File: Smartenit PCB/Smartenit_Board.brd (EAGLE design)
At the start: 54.9 x 71.8 mm, 86 parts, among them J1 2X5CONNECTOR1.27MM, Q1 QUARTZ_3.58M_2PIN, U1 SN74LVC1G3157, U2 ADE7953, U3 ESP-WROOM-32

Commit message: Fixed Silk Screen final before sending to Al
fixed silk screen and renumbered parts
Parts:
- renumbered LD100 to R/G_LED, LED100 to BLUE_LED
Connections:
- net ADC1 renamed PILOT_READ
- net DIO0 renamed CS
- net DIO1 renamed MPLEX
- net DIO10 renamed GFI_TEST
- net DIO13 renamed PILOT_GEN
- net DIO16 renamed GREEN_LED
- net DIO17 renamed RED_LED
- net DIO8 renamed BUTTON
- net DIO9 renamed BLUE_LED
- net N$30 renamed GPIO2
- net 3.3V: no longer R15.1
- net GND: now also R15.1
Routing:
- net 3.3V: track 221.8 -> 217.6 mm
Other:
- board text added: "C:/Users/Brandon/Desktop/Fall 2017/EECS 159A (SENIOR DESIGN)/chipart_00000.bmp"

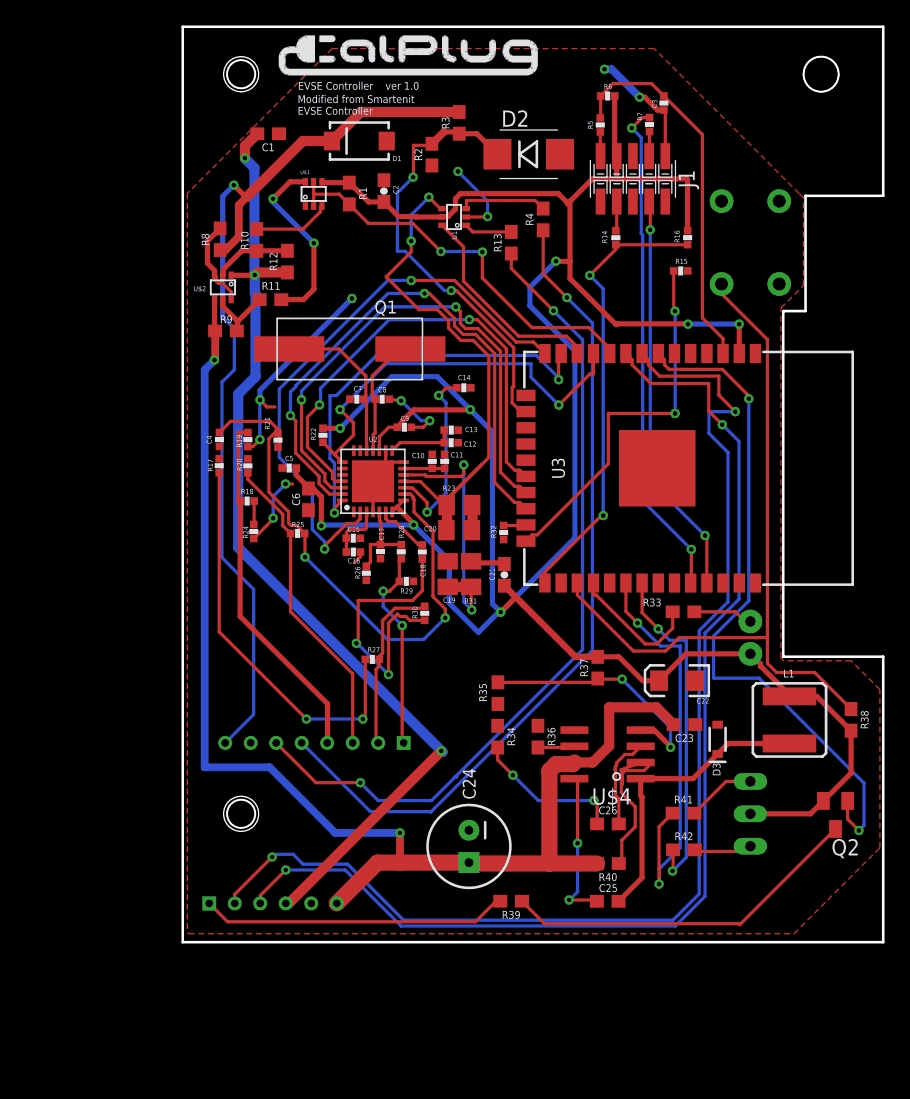
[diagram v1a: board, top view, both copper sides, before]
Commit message: Changed ground planes
separated into analog and digital grounds. Rearachnged layout for better coupling.
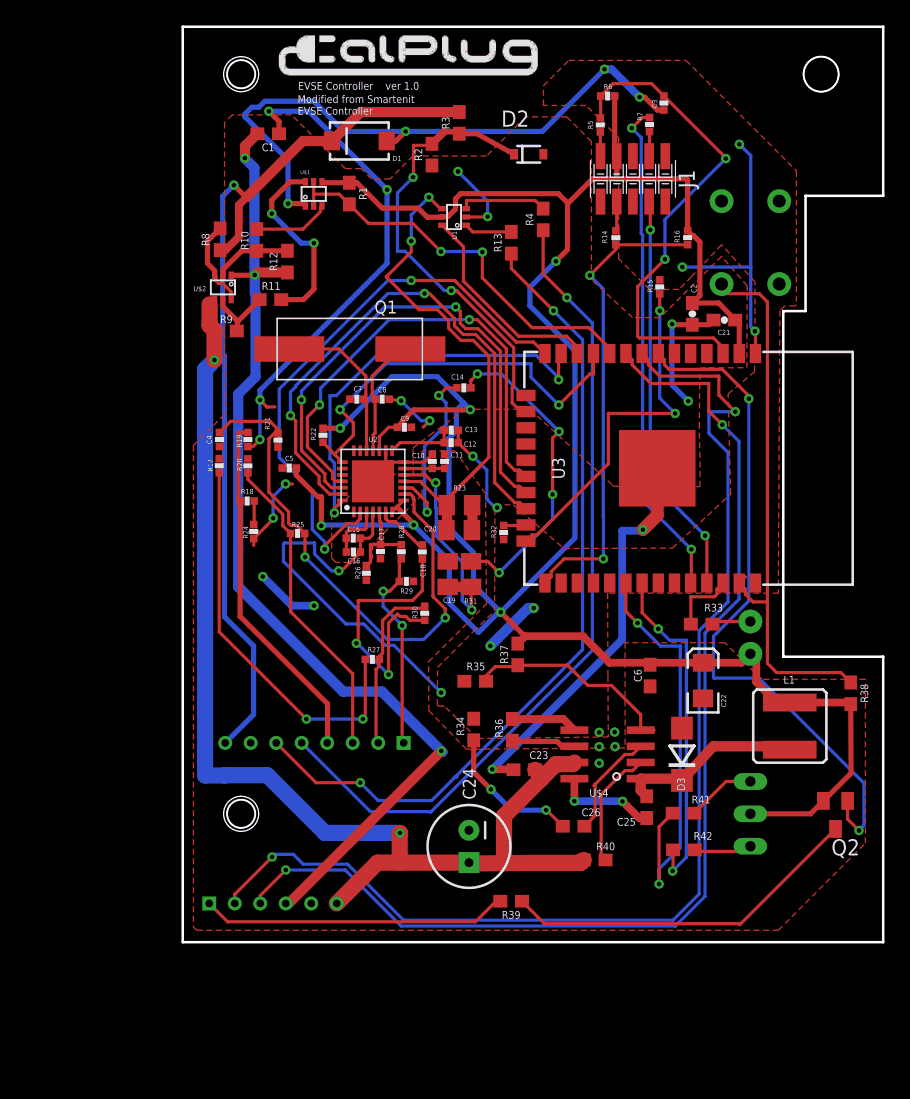
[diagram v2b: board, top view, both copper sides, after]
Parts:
- C22: value (none) -> 10uF
- C24: value (none) -> 100uF
- D2: device SparkFun:DIODE-HV -> SparkFun:SOD-323
- D3: device SparkFun-DiscreteSemi:SOD-323 -> diode:DO214BA
- moved C6 30.1 mm to (36.7, -50.9)
- moved C21 26.4 mm to (42.5, -23.0), turned to 180 degrees
- moved C2 26.0 mm to (40.0, -22.5), turned to 270 degrees
- moved C23 13.0 mm to (26.8, -58.3), turned to 0 degrees
- moved C25 8.00 mm to (36.4, -61.2), turned to 90 degrees
- moved R37 6.36 mm to (26.3, -49.2)
- moved D3 3.03 mm to (39.2, -57.1)
- moved C26 2.70 mm to (30.7, -62.7)
- moved R38 2.08 mm to (52.4, -52.3)
- moved R36 2.08 mm to (25.9, -55.1)
- moved R15 2.07 mm to (37.4, -20.4), turned to 270 degrees
- moved C22 2.05 mm to (40.8, -51.3), turned to 90 degrees
- moved R35 2.01 mm to (22.9, -51.3), turned to 0 degrees
- moved R34 1.96 mm to (22.8, -55.1)
- moved R33 1.72 mm to (40.7, -46.9)
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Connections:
- removed net GND: C1.1, C10.2, C11.2, C12.1, C13.1, C14.2, C15.1, C16.1, C17.1, C18.2, C19.2, C2.2, C20.2, C21.2, C22.C, C23.1, C24.2, C3.1, C4.1, C5.1, C6.1, C7.1, C8.1, C9.1, D1.A, D2.A, D3.A, J1.10, R15.1, R17.2, R19.2, R2.1, R20.1, R21.1, R23.2, R24.2, R26.1, R29.1, R30.2, R31.2, R32.1, R34.1, R35.1, R36.1, S100.1, U$1.1, U$3.7, U$4.5, U$5.5, U1.2, U2.14, U2.16, U2.4, U2.PAD, U3.1, U3.15, U3.38, U3.GND
- new net AGND: C1.1, C10.2, C11.2, C14.2, C17.1, C18.2, C19.2, C2.2, C20.2, C21.2, C22.C, C23.1, C24.2, C4.1, C5.1, C6.1, C7.1, C8.1, C9.1, D2.2, D3.A, R17.2, R19.2, R2.1, R20.1, R21.1, R23.2, R24.2, R26.1, R29.1, R30.2, R31.2, U$3.7, U$5.5, U1.2, U2.14, U2.16, U2.PAD, U3.15, U3.GND
- new net DGND: C12.1, C13.1, C15.1, C16.1, C3.1, D1.A, J1.10, R15.1, R32.1, R34.1, R35.1, R36.1, S100.1, U$1.1, U$4.5, U2.4, U3.1, U3.38
- net BLUE_LED: now also U3.36; no longer U3.28
- net BUTTON: now also U3.37; no longer U3.27
- net PILOT_READ: now also D2.1; no longer D2.C
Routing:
- net AGND: track 0.00 -> 164.2 mm, vias 0 -> 22
- net DGND: track 0.00 -> 119.2 mm, vias 0 -> 13
- net GND: track 81.8 -> 0.00 mm, vias 13 -> 0
- net BUTTON: track 57.4 -> 43.9 mm
- net NRST: track 29.6 -> 38.7 mm, vias 0 -> 2
- net N$18: track 23.2 -> 14.6 mm
- net 12V: track 100.2 -> 93.1 mm
- net BLUE_LED: track 10.5 -> 5.35 mm
- net 3.3V: track 217.6 -> 212.8 mm, vias 8 -> 6
- net N$14: track 13.5 -> 9.42 mm
- net N$22: track 12.1 -> 8.34 mm
- net V2P: track 20.9 -> 17.6 mm
- net N$19: track 19.8 -> 16.8 mm, vias 2 -> 0
- net N$4: track 2.90 -> 5.18 mm
- net GPIO0: track 35.4 -> 37.2 mm
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- added copper zone on layer 1, net AGND
- added copper zone on layer 1, net DGND
- removed copper zone on layer 1, net GND

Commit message: minor changes to ground planes
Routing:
- net AGND: track 164.2 -> 149.1 mm
- net DGND: track 119.2 -> 104.3 mm
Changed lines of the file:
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@@
 <contactref element="C4" pad="2"/>
 <contactref element="U2" pad="9"/>
-<via x="9.59" y="-41.59" extent="1-16" drill="0.35"/>
 <wire x1="19.648" y1="-44.71751875" x2="19.648" y2="-44.658" width="0.254" layer="1"/>
 <wire x1="19.648" y1="-44.658" x2="19.63" y2="-44.64" width="0.254" layer="1"/>
@@
 <wire x1="19.63" y1="-39.55" x2="18.14" y2="-38.06" width="0.254" layer="1"/>
 <wire x1="18.14" y1="-37.07560625" x2="18.14" y2="-38.06" width="0.254" layer="1"/>
-<wire x1="9.59" y1="-41.59" x2="9.59" y2="-39.77" width="0.254" layer="1"/>
-<wire x1="9.59" y1="-39.77" x2="9.56" y2="-39.74" width="0.254" layer="1"/>
+<wire x1="9.59" y1="-39.77" x2="9.5734" y2="-39.7534" width="0.254" layer="1"/>
+<wire x1="9.5734" y1="-39.7534" x2="9.56" y2="-39.74" width="0.254" layer="1"/>
 <wire x1="2.88" y1="-31.82" x2="3.75" y2="-30.95" width="0.254" layer="1"/>
 <wire x1="3.75" y1="-30.95" x2="6.84" y2="-30.95" width="0.254" layer="1"/>
@@
 <wire x1="6.7584" y1="-32.31" x2="7.2084" y2="-31.86" width="0.254" layer="1"/>
 <wire x1="7.2084" y1="-31.86" x2="7.47" y2="-31.86" width="0.254" layer="1"/>
-<wire x1="9.59" y1="-41.59" x2="16.06" y2="-48.06" width="0.254" layer="16"/>
-<wire x1="18.89" y1="-48.06" x2="20.59" y2="-46.36" width="0.254" layer="16"/>
-<wire x1="16.06" y1="-48.06" x2="18.89" y2="-48.06" width="0.254" layer="16"/>
+<wire x1="20.59" y1="-46.36" x2="18.89" y2="-48.06" width="0.254" layer="16"/>
 <wire x1="18.0752" y1="-36.864225" x2="18.0752" y2="-37.01080625" width="0.254" layer="1"/>
 <wire x1="17.32" y1="-36.651" x2="17.861975" y2="-36.651" width="0.254" layer="1"/>
@@
 <wire x1="8.3072" y1="-38.05061875" x2="6.7584" y2="-36.50181875" width="0.254" layer="1"/>
 <wire x1="6.7584" y1="-36.50181875" x2="6.7584" y2="-32.31" width="0.254" layer="1"/>
+<wire x1="18.89" y1="-48.06" x2="16.82" y2="-48.06" width="0.254" layer="16"/>
+<wire x1="16.82" y1="-48.06" x2="14.3414" y2="-45.6322" width="0.254" layer="16"/>
+<via x="14.3414" y="-45.6322" extent="1-16" drill="0.35"/>
+<wire x1="14.3414" y1="-45.6322" x2="12.8154" y2="-45.6322" width="0.254" layer="1"/>
+<wire x1="12.8154" y1="-45.6322" x2="9.6012" y2="-42.418" width="0.254" layer="1"/>
+<wire x1="9.6012" y1="-42.418" x2="9.6012" y2="-39.7812" width="0.254" layer="1"/>
+<wire x1="9.6012" y1="-39.7812" x2="9.59" y2="-39.77" width="0.254" layer="1"/>
 </signal>
 <signal name="N$11">
@@
 <wire x1="5.015" y1="-13.365" x2="9.42" y2="-8.96" width="0.8" layer="1"/>
 <wire x1="9.42" y1="-8.96" x2="11.7" y2="-8.96" width="0.8" layer="1"/>
-<wire x1="11.7" y1="-8.96" x2="13.97" y2="-6.69" width="0.8" layer="1"/>
+<wire x1="11.7" y1="-8.96" x2="12.5906" y2="-8.0694" width="0.8" layer="1"/>
+<wire x1="12.5906" y1="-8.0694" x2="13.97" y2="-6.69" width="0.8" layer="1"/>
 <wire x1="13.97" y1="-6.69" x2="21.69" y2="-6.69" width="0.8" layer="1"/>
 <wire x1="3.13" y1="-22.76" x2="3.13" y2="-25.67040625" width="0.4064" layer="16"/>
@@
 <contactref element="R26" pad="1"/>
 <contactref element="R17" pad="2"/>
-<wire x1="18.791" y1="-41.744" x2="18.791" y2="-44.229" width="0.254" layer="1"/>
-<wire x1="18.02" y1="-45" x2="13.76" y2="-45" width="0.254" layer="1"/>
-<wire x1="13.76" y1="-45" x2="13.76" y2="-48.22" width="0.254" layer="1"/>
 <wire x1="13.76" y1="-48.22" x2="13.62" y2="-48.36" width="0.254" layer="1"/>
 <via x="13.62" y="-48.36" extent="1-16" drill="0.35"/>
 <wire x1="13.62" y1="-48.36" x2="13.69" y2="-48.36" width="0.254" layer="16"/>
-<wire x1="13.69" y1="-48.36" x2="16.14" y2="-50.81" width="0.254" layer="16"/>
 <via x="16.14" y="-50.81" extent="1-16" drill="0.35"/>
 <wire x1="16.14" y1="-50.81" x2="16.14" y2="-46.76" width="0.254" layer="1"/>
@@
 <wire x1="17.50343125" y1="-46.2516" x2="17.80183125" y2="-46.55" width="0.254" layer="1"/>
 <wire x1="17.80183125" y1="-46.55" x2="18.98" y2="-46.55" width="0.254" layer="1"/>
-<wire x1="18.791" y1="-44.229" x2="18.02" y2="-45" width="0.254" layer="1"/>
 <contactref element="C14" pad="2"/>
 <contactref element="C4" pad="1"/>
@@
 <via x="16.0274" y="-12.7762" extent="1-16" drill="0.35"/>
 <wire x1="6.06" y1="-28.52" x2="16.0274" y2="-18.5526" width="0.4064" layer="16"/>
-<wire x1="16.0274" y1="-12.7762" x2="9.8806" y2="-6.6294" width="0.4064" layer="16"/>
-<wire x1="9.8806" y1="-6.6294" x2="6.7564" y2="-6.6294" width="0.4064" layer="16"/>
-<via x="6.7564" y="-6.6294" extent="1-16" drill="0.35"/>
-<wire x1="6.7564" y1="-6.6294" x2="7.55" y2="-7.423" width="0.4064" layer="1"/>
 <wire x1="7.55" y1="-7.423" x2="7.55" y2="-8.39" width="0.4064" layer="1"/>
 <wire x1="41.632" y1="-23.0046" x2="41.269" y2="-23.3676" width="0.4064" layer="1"/>
@@
 <wire x1="36.0934" y1="-39.4462" x2="37.22" y2="-38.3196" width="1.016" layer="1"/>
 <wire x1="37.22" y1="-38.3196" x2="37.22" y2="-34.63" width="1.016" layer="1"/>
+<wire x1="13.62" y1="-48.36" x2="16.07" y2="-50.81" width="0.4064" layer="16"/>
+<wire x1="16.07" y1="-50.81" x2="16.14" y2="-50.81" width="0.4064" layer="16"/>
+<wire x1="16.0274" y1="-12.7762" x2="11.1506" y2="-7.8994" width="0.6096" layer="16"/>
+<wire x1="11.1506" y1="-7.8994" x2="9.2202" y2="-7.8994" width="0.6096" layer="16"/>
+<via x="9.2202" y="-7.8994" extent="1-16" drill="0.35"/>
 </signal>
 <signal name="DGND">
@@
 <wire x1="12.462" y1="-42.672" x2="12.2428" y2="-42.672" width="0.254" layer="1"/>
 <via x="12.2428" y="-42.672" extent="1-16" drill="0.35"/>
-<wire x1="12.2428" y1="-42.672" x2="11.6586" y2="-42.672" width="0.254" layer="16"/>
-<wire x1="10.3378" y1="-41.3512" x2="10.3378" y2="-40.4876" width="0.254" layer="16"/>
-<wire x1="10.3378" y1="-40.4876" x2="7.9756" y2="-40.4876" width="0.254" layer="16"/>
-<wire x1="7.9756" y1="-40.4876" x2="7.8994" y2="-40.5638" width="0.254" layer="16"/>
-<wire x1="7.8994" y1="-40.5638" x2="7.8994" y2="-41.9354" width="0.254" layer="16"/>
 <via x="20.2692" y="-52.2224" extent="1-16" drill="0.35"/>
-<wire x1="14.19101875" y1="-46.8376" x2="15.87061875" y2="-48.5172" width="0.254" layer="16"/>
-<wire x1="16.564" y1="-48.5172" x2="20.2692" y2="-52.2224" width="0.254" layer="16"/>
-<wire x1="15.87061875" y1="-48.5172" x2="16.564" y2="-48.5172" width="0.254" layer="16"/>
-<wire x1="12.8016" y1="-46.8376" x2="14.19101875" y2="-46.8376" width="0.254" layer="16"/>
-<wire x1="11.6586" y1="-42.672" x2="10.3378" y2="-41.3512" width="0.254" layer="16"/>
-<wire x1="7.8994" y1="-41.9354" x2="12.8016" y2="-46.8376" width="0.254" layer="16"/>
 <polygon width="0.254" layer="1">
-<vertex x="23.114" y="-55.8292"/>
-<vertex x="20.5232" y="-53.2892"/>
-<vertex x="20.0406" y="-53.2892"/>
-<vertex x="19.9644" y="-53.213"/>
-<vertex x="19.9898" y="-50.2412"/>
-<vertex x="22.8092" y="-47.4218"/>
-<vertex x="24.4602" y="-45.8216"/>
+<vertex x="23.114" y="-55.4736"/>
+<vertex x="20.5994" y="-52.959"/>
+<vertex x="20.5486" y="-52.8066"/>
+<vertex x="20.5486" y="-50.419"/>
+<vertex x="22.9616" y="-47.9552"/>
+<vertex x="24.4602" y="-46.3804"/>
 <vertex x="24.4856" y="-37.4904"/>
 <vertex x="25.9334" y="-37.4904"/>
@@
 <vertex x="46.7106" y="-44.3992"/>
 <vertex x="46.736" y="-44.4246"/>
-<vertex x="33.3248" y="-44.4246"/>
-<vertex x="33.3502" y="-50.9524"/>
-<vertex x="33.3756" y="-55.7022"/>
+<vertex x="31.5214" y="-44.3992"/>
+<vertex x="31.496" y="-50.9524"/>
+<vertex x="31.5214" y="-55.3974"/>
 </polygon>
 <wire x1="21.608" y1="-31.638" x2="21.608" y2="-32.619" width="0.254" layer="1"/>
@@
 <wire x1="9.4284" y1="-13.8684" x2="8.255" y2="-13.8684" width="0.4064" layer="1"/>
 <via x="8.255" y="-13.8684" extent="1-16" drill="0.35"/>
-<wire x1="8.255" y1="-13.8684" x2="8.255" y2="-10.4394" width="0.4064" layer="16"/>
-<wire x1="8.255" y1="-10.4394" x2="4.8768" y2="-7.0612" width="0.4064" layer="16"/>
-<wire x1="4.8768" y1="-7.0612" x2="4.8768" y2="-6.8476" width="0.4064" layer="16"/>
-<wire x1="4.8768" y1="-6.8476" x2="5.4102" y2="-6.3142" width="0.4064" layer="16"/>
-<wire x1="5.4102" y1="-6.3142" x2="5.96200625" y2="-6.3142" width="0.4064" layer="16"/>
-<wire x1="5.96200625" y1="-6.3142" x2="6.43140625" y2="-5.8448" width="0.4064" layer="16"/>
-<wire x1="6.43140625" y1="-5.8448" x2="10.2898" y2="-5.8448" width="0.4064" layer="16"/>
-<wire x1="12.6492" y1="-8.2042" x2="17.4752" y2="-8.2042" width="0.4064" layer="16"/>
+<wire x1="8.255" y1="-10.4394" x2="8.255" y2="-13.8684" width="0.4064" layer="16"/>
+<wire x1="17.4752" y1="-8.2042" x2="12.6492" y2="-8.2042" width="0.4064" layer="16"/>
 <via x="17.4752" y="-8.2042" extent="1-16" drill="0.35"/>
 <wire x1="17.4752" y1="-8.2042" x2="16.7194" y2="-8.96" width="0.4064" layer="1"/>
 <wire x1="16.7194" y1="-8.96" x2="16" y2="-8.96" width="0.4064" layer="1"/>
-<wire x1="10.2898" y1="-5.8448" x2="12.6492" y2="-8.2042" width="0.4064" layer="16"/>
 <wire x1="17.4752" y1="-8.2042" x2="28.2058" y2="-8.2042" width="0.4064" layer="16"/>
 <wire x1="28.2058" y1="-8.2042" x2="33.08" y2="-3.33" width="0.4064" layer="16"/>
@@
 <wire x1="24.13" y1="-48.5648" x2="27.1018" y2="-45.593" width="0.8128" layer="16"/>
 <wire x1="27.1018" y1="-45.593" x2="27.5336" y2="-45.593" width="0.8128" layer="16"/>
+<wire x1="12.2428" y1="-42.672" x2="12.2428" y2="-45.1866" width="0.4064" layer="16"/>
+<wire x1="12.2428" y1="-45.1866" x2="15.651859375" y2="-48.595659375" width="0.4064" layer="16"/>
+<wire x1="15.651859375" y1="-48.595659375" x2="16.642459375" y2="-48.595659375" width="0.4064" layer="16"/>
+<wire x1="16.642459375" y1="-48.595659375" x2="20.2692" y2="-52.2224" width="0.4064" layer="16"/>
+<wire x1="12.6492" y1="-8.2042" x2="11.2522" y2="-6.8072" width="0.4064" layer="16"/>
+<wire x1="11.2522" y1="-6.8072" x2="7.5438" y2="-6.8072" width="0.4064" layer="16"/>
+<wire x1="7.5438" y1="-6.8072" x2="7.5438" y2="-9.7282" width="0.4064" layer="16"/>
+<wire x1="7.5438" y1="-9.7282" x2="8.255" y2="-10.4394" width="0.4064" layer="16"/>
 </signal>
 <signal name="N$30">
